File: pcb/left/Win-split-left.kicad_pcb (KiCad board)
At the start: 2 copper layers, 212.5 x 118.3 mm, 157 parts, among them J1 Conn_01x04_Socket, Q1 Q_PMOS_GSD, SW8 ROT_SKYLOONG_HS, U1 RP2040_ProMicro, U3 74AHCT1G125

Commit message: designed
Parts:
- moved C29 55.9 mm to (148.9, 216.2), turned to -166 degrees
- moved LED29 55.1 mm to (154.1, 215.7), turned to -166 degrees
- moved MX29 54.3 mm to (152.8, 210.8), turned to -166 degrees
- moved D29 52.1 mm to (160.6, 205.3), turned to -76 degrees
- moved H4 50.5 mm to (162.2, 198.6), turned to 0 degrees
- moved C30 48.6 mm to (192.8, 205.2), turned to -166 degrees
- moved LED30 48.1 mm to (198.0, 204.7), turned to -166 degrees
- moved C22 47.1 mm to (153.6, 175.8), turned to -166 degrees
- moved MX30 47.1 mm to (196.7, 199.8), turned to -166 degrees
- moved LED22 46.2 mm to (158.7, 175.3), turned to -166 degrees
- moved MX22 45.4 mm to (157.5, 170.3), turned to -166 degrees
- moved D30 45.1 mm to (204.5, 194.3), turned to -76 degrees
- moved C8 44.8 mm to (130.5, 142.3), turned to -166 degrees
- moved LED23 44.7 mm to (191.0, 186.8), turned to -166 degrees
- moved C23 44.1 mm to (196.3, 186.3), turned to 14 degrees
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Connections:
- U1 pad 12: ROTB -> ROTA
- U1 pad 13: ROTA -> ROTB
- U1 pad 20: COL2 -> COL5
- U1 pad 21: COL0 -> COL3
- U1 pad 22: COL3 -> COL0
- U1 pad 23: COL1 -> COL4
- U1 pad 26: COL4 -> COL2
- U1 pad 27: COL5 -> COL1
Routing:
- net +5V: track 972.4 -> 1046.9 mm, vias 8 -> 6
- net COL0: track 362.6 -> 434.1 mm, vias 1 -> 9
- net COL2: track 205.2 -> 248.7 mm, vias 2 -> 4
- net COL1: track 252.4 -> 292.6 mm, vias 2 -> 4
- net ROTB: track 190.8 -> 222.3 mm, vias 4 -> 0
- net ROTA: track 192.0 -> 222.6 mm, vias 5 -> 0
- net VCC: track 228.8 -> 257.9 mm, vias 2 -> 3
- net ROW4: track 232.6 -> 244.2 mm
- net ROW3: track 197.6 -> 206.7 mm
- net COL6: track 139.8 -> 148.8 mm
- net Net-(LED33-DIN): track 30.3 -> 38.0 mm
- net COL3: track 208.8 -> 201.8 mm
- net COL4: track 198.7 -> 192.6 mm
- net ROW1: track 192.0 -> 198.0 mm
- net Net-(LED15-DIN): track 27.9 -> 32.9 mm
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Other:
- board size 212.5 x 118.3 mm -> 213.2 x 120.4 mm

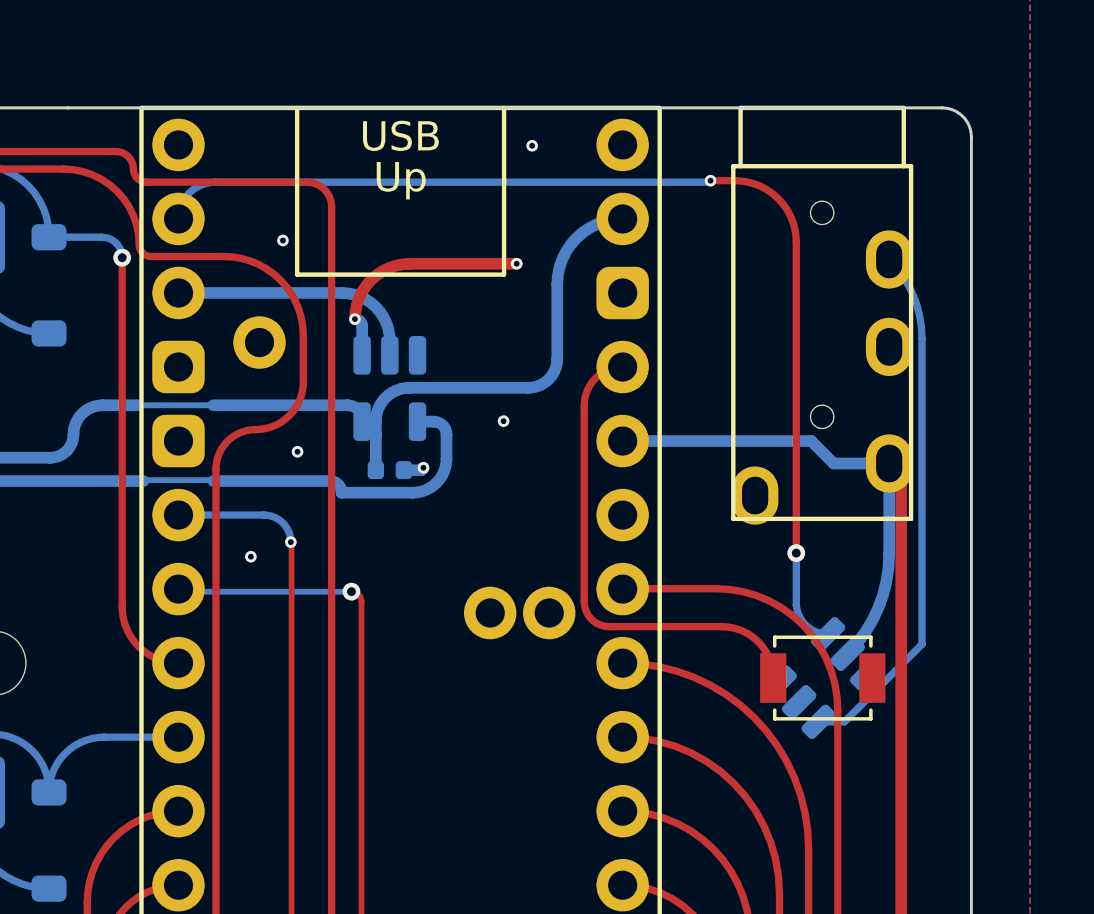
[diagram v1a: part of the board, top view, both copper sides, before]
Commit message: vial firmware and 3D cases
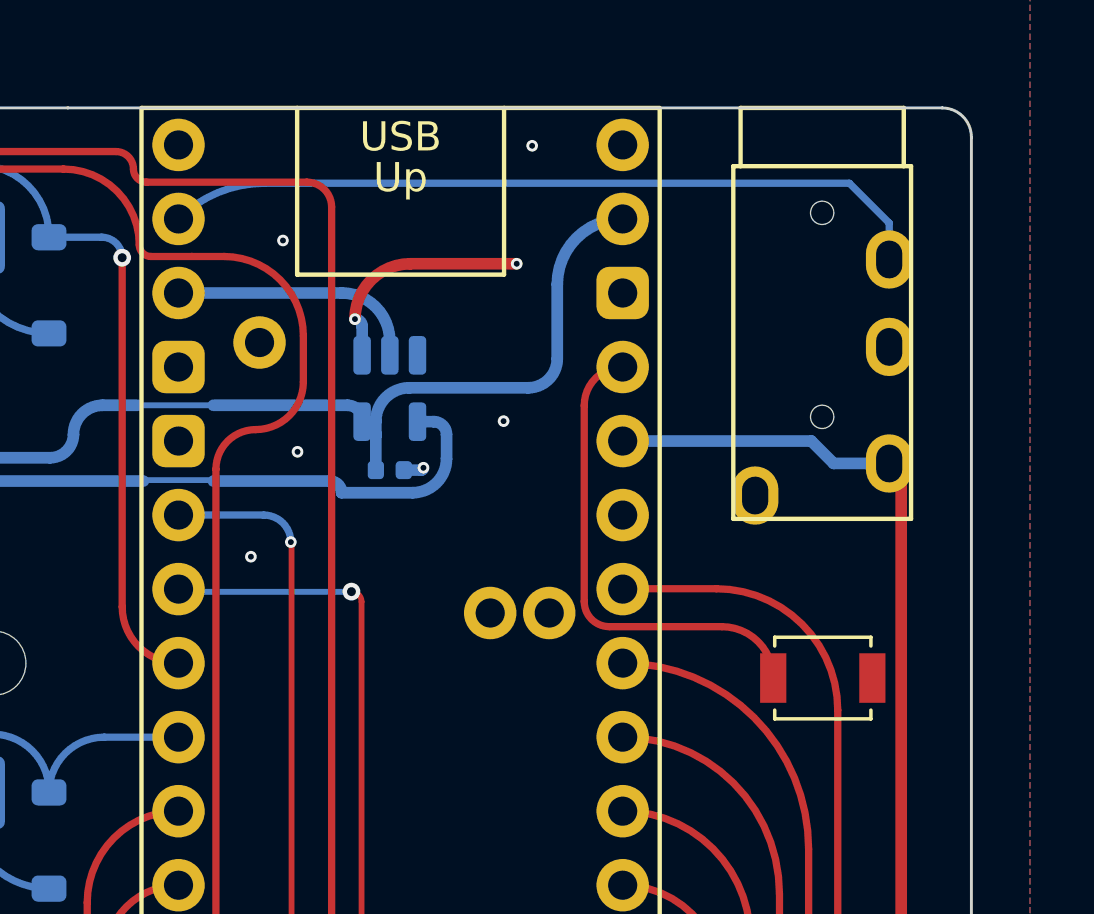
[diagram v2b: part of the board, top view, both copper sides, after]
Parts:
- removed ESD1: SRV05-4, PCM_marbastlib-various:SOT-23-6-routable
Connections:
- TRRS1 pad 4: Net-(ESD1-IO1) -> DATA
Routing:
- net Net-(ESD1-IO1): track 18.1 -> 0.00 mm
- net DATA: track 37.0 -> 26.5 mm, vias 2 -> 0
- net VCC: track 257.9 -> 251.0 mm
